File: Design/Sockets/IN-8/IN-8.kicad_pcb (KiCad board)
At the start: 2 copper layers, 180 x 41 mm, 20 parts, among them J1 Conn_01x12_Male, J2 Conn_01x12_Male, J3 Conn_01x12_Male, J4 Conn_01x12_Male, J5 Conn_01x12_Male, J6 Conn_01x12_Male, U1 IN-8, U2 IN-8, U3 IN-8, U4 IN-8, U5 IN-8, U6 IN-8

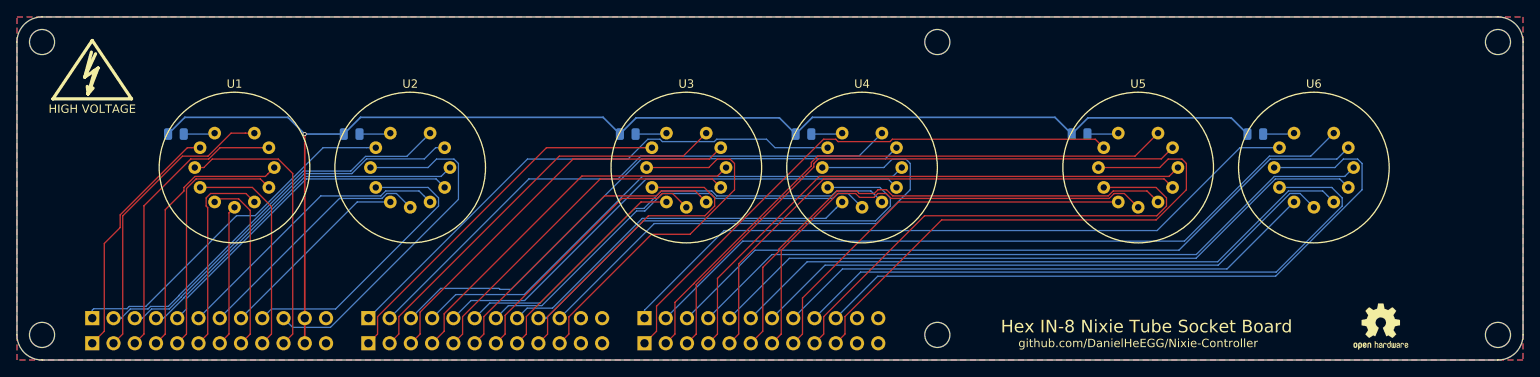
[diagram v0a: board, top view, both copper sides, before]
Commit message: Fix IN-8 socket board orientation issue
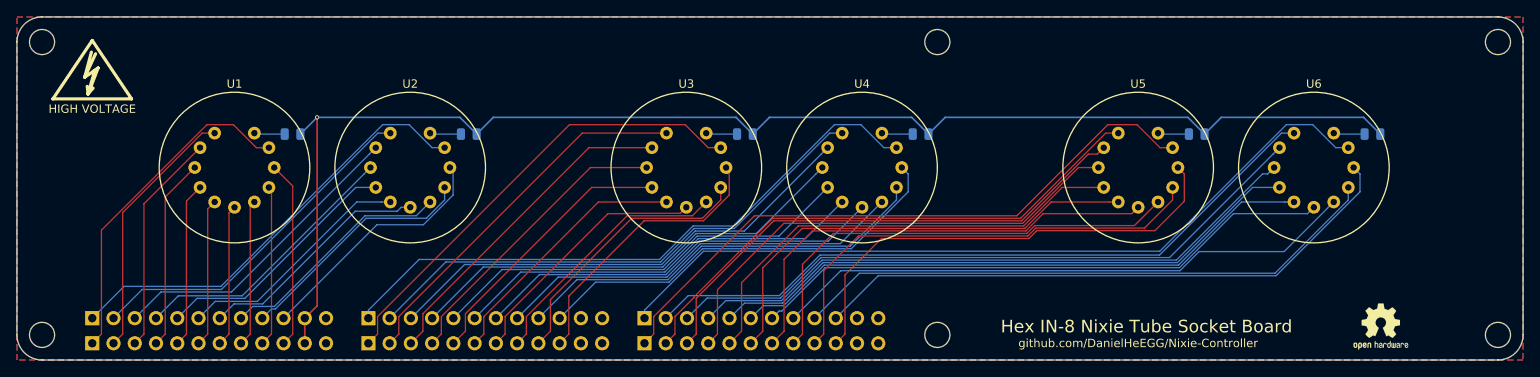
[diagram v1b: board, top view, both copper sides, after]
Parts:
- moved R2 14.0 mm to (121.0, 74.0), turned to 180 degrees
- moved R3 14.0 mm to (154.0, 74.0), turned to 180 degrees
- moved R4 14.0 mm to (175.0, 74.0), turned to 180 degrees
- moved R5 14.0 mm to (208.0, 74.0), turned to 180 degrees
- moved R6 14.0 mm to (229.0, 74.0), turned to 180 degrees
- moved R1 13.9 mm to (99.9, 74.0), turned to 180 degrees
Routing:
- net Net-(J2-Pad10): track 43.1 -> 29.8 mm
- net Net-(J4-Pad10): track 62.5 -> 51.1 mm
- net Net-(J6-Pad10): track 83.5 -> 72.1 mm
- net Net-(J1-Pad10): track 33.6 -> 22.4 mm
- net Net-(J1-Pad1): track 29.6 -> 40.3 mm
- net Net-(J5-Pad5): track 66.4 -> 55.8 mm
- net Net-(J6-Pad1): track 84.9 -> 95.4 mm
- net Net-(J3-Pad1): track 44.8 -> 55.3 mm
- net Net-(J5-Pad4): track 68.7 -> 58.4 mm
- net Net-(J3-Pad10): track 44.0 -> 33.7 mm
- net Net-(J4-Pad1): track 64.4 -> 74.4 mm
- net Net-(J2-Pad1): track 42.9 -> 52.8 mm
- net Net-(J1-Pad5): track 29.7 -> 19.8 mm
- net Net-(J2-Pad5): track 40.0 -> 30.2 mm
- net Net-(J2-Pad4): track 42.6 -> 33.1 mm
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
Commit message: Add license notice to all human readable files
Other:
- board text added: "IN-8 Nixie Socket PCB Copyright (C) 2020 Daniel He See <https://www.gnu.org/licenses/>."
- board text added: "IN-8 Nixie Socket PCB Copyright (C) 2020 Daniel He This program is free software: you can redistribute it and/or modify it under the terms of the GNU General Public License as published by the Free Software Foundation, either version 3 of the License, or (at your option) any later version. This program is distributed in the hope that it will be useful, but WITHOUT ANY WARRANTY; without even the i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"
